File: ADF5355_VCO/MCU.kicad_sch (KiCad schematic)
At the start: 34 parts, among them SW2 SW_Push, SW3 SW_DPDT_x2, U2 STM32L433CCTx, Y1 8MHz, Y2 32kHz

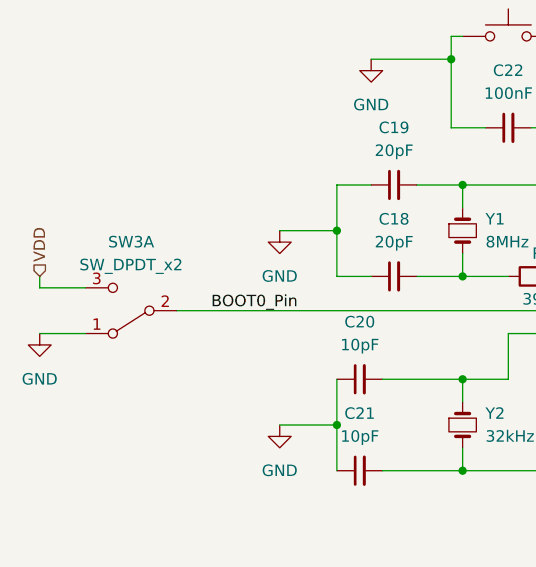
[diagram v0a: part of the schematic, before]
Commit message: Removed the switch from power supply
Removed the switch from the main power supply and changed the switch on the boot pin to SDPT switch
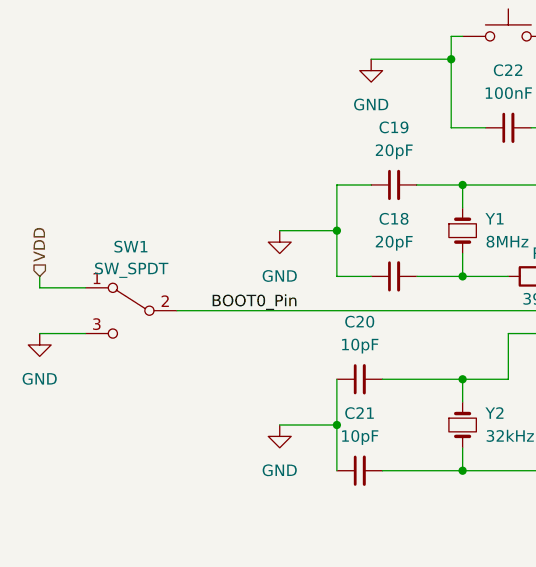
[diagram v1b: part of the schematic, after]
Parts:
- removed SW3: SW_DPDT_x2, symbol Switch:SW_DPDT_x2
- added SW1: SW_SPDT, symbol Switch:SW_SPDT
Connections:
- net BOOT0_Pin: now also SW1.2 (B)
- net GND: now also SW1.3 (C)
- net VDD: now also SW1.1 (A)
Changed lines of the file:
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@@
+    )
+  )
+  (symbol (lib_id "Switch:SW_SPDT") (at 34.29 78.74 0) (mirror y) (unit 1)
+    (in_bom yes) (on_board yes) (dnp no)
+    (property "Reference" "SW1" (at 34.29 71.6747 0)
+      (effects (font (size 1.27 1.27)))
+    )
+    (property "Value" "SW_SPDT" (at 34.29 74.0989 0)
+      (effects (font (size 1.27 1.27)))
+    )
+    (property "Footprint" "" (at 34.29 78.74 0)
+      (effects (font (size 1.27 1.27)) hide)
+    )
+    (property "Datasheet" "~" (at 34.29 78.74 0)
+      (effects (font (size 1.27 1.27)) hide)
+    )
+    (pin "1")
+    (pin "2")
+    (pin "3")
+    (instances
+      (project "ADF5355_VCO"
+        (path "/29349b68-071c-451b-9b1e-10b5ef7e12a6/8e6d62a1-615e-4e74-ad33-9284c4715f87"
+          (reference "SW1") (unit 1)
+        )
+      )
     )
   )
@@
         )
       )
-    )
-  )
-  (symbol (lib_id "Switch:SW_DPDT_x2") (at 34.29 78.74 180) (unit 1)
-    (in_bom yes) (on_board yes) (dnp no) (fields_autoplaced)
-    (property "Reference" "SW3" (at 34.29 71.12 0)
-      (effects (font (size 1.27 1.27)))
-    )
-    (property "Value" "SW_DPDT_x2" (at 34.29 73.66 0)
-      (effects (font (size 1.27 1.27)))
-    )
-    (property "Footprint" "" (at 34.29 78.74 0)
-      (effects (font (size 1.27 1.27)) hide)
-    )
-    (property "Datasheet" "~" (at 34.29 78.74 0)
-      (effects (font (size 1.27 1.27)) hide)
-    )
-    (pin "1")
-    (pin "2")
-    (pin "3")
-    (pin "4")
-    (pin "5")
-    (pin "6")
-    (instances
-      (project "ADF5355_VCO"
-        (path "/29349b68-071c-451b-9b1e-10b5ef7e12a6/8e6d62a1-615e-4e74-ad33-9284c4715f87"
-          (reference "SW3") (unit 1)
-        )
-      )

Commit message: Added PLL filter
Added components for the PLL filter
 according to the components on evaluation board

Added specific components to BOM
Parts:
- C18, C19, C20, C21: footprint (none) -> Capacitor_SMD:C_0603_1608Metric_Pad1.08x0.95mm_HandSolder
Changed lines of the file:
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@@
       (effects (font (size 1.27 1.27)))
     )
-    (property "Footprint" "" (at 63.5 64.77 0)
+    (property "Footprint" "Capacitor_SMD:C_0603_1608Metric_Pad1.08x0.95mm_HandSolder" (at 63.5 64.77 0)
       (effects (font (size 1.27 1.27)) hide)
     )
@@
       (effects (font (size 1.27 1.27)))
     )
-    (property "Footprint" "" (at 63.5 74.93 0)
+    (property "Footprint" "Capacitor_SMD:C_0603_1608Metric_Pad1.08x0.95mm_HandSolder" (at 63.5 74.93 0)
       (effects (font (size 1.27 1.27)) hide)
     )
@@
       (effects (font (size 1.27 1.27)))
     )
-    (property "Footprint" "" (at 59.69 96.52 0)
+    (property "Footprint" "Capacitor_SMD:C_0603_1608Metric_Pad1.08x0.95mm_HandSolder" (at 59.69 96.52 0)
       (effects (font (size 1.27 1.27)) hide)
     )
@@
       (effects (font (size 1.27 1.27)))
     )
-    (property "Footprint" "" (at 59.69 86.36 0)
-      (effects (font (size 1.27 1.27)) hide)
-    )
+    (property "Footprint" "Capacitor_SMD:C_0603_1608Metric_Pad1.08x0.95mm_HandSolder" (at 59.69 86.36 0)
+      (effects (font (size 1.27 1.27)) hide)
+    )

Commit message: Added TCXO and remaining footprints
Added remaining footprints
    NX3225GD
    710X toggle switch
    SMT button

Added ClearClock AX3 TCXO symbol and footprint

Added TCXO schematic with 3 options:
    LVPECL, LVDS and HCSL
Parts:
- FB1, R1: footprint (none) -> Resistor_SMD:R_0603_1608Metric_Pad0.98x0.95mm_HandSolder
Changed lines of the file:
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@@
       (effects (font (size 1.27 1.27)))
     )
-    (property "Footprint" "" (at 114.3 52.578 90)
+    (property "Footprint" "Resistor_SMD:R_0603_1608Metric_Pad0.98x0.95mm_HandSolder" (at 114.3 52.578 90)
       (effects (font (size 1.27 1.27)) hide)
     )
@@
       (effects (font (size 1.27 1.27)))
     )
-    (property "Footprint" "" (at 80.01 76.708 90)
-      (effects (font (size 1.27 1.27)) hide)
-    )
+    (property "Footprint" "Resistor_SMD:R_0603_1608Metric_Pad0.98x0.95mm_HandSolder" (at 80.01 76.708 90)
+      (effects (font (size 1.27 1.27)) hide)
+    )
